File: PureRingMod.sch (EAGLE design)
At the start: 31 parts, among them IC1 TL074P, IC2 TL072P, X1 NC3FD-V

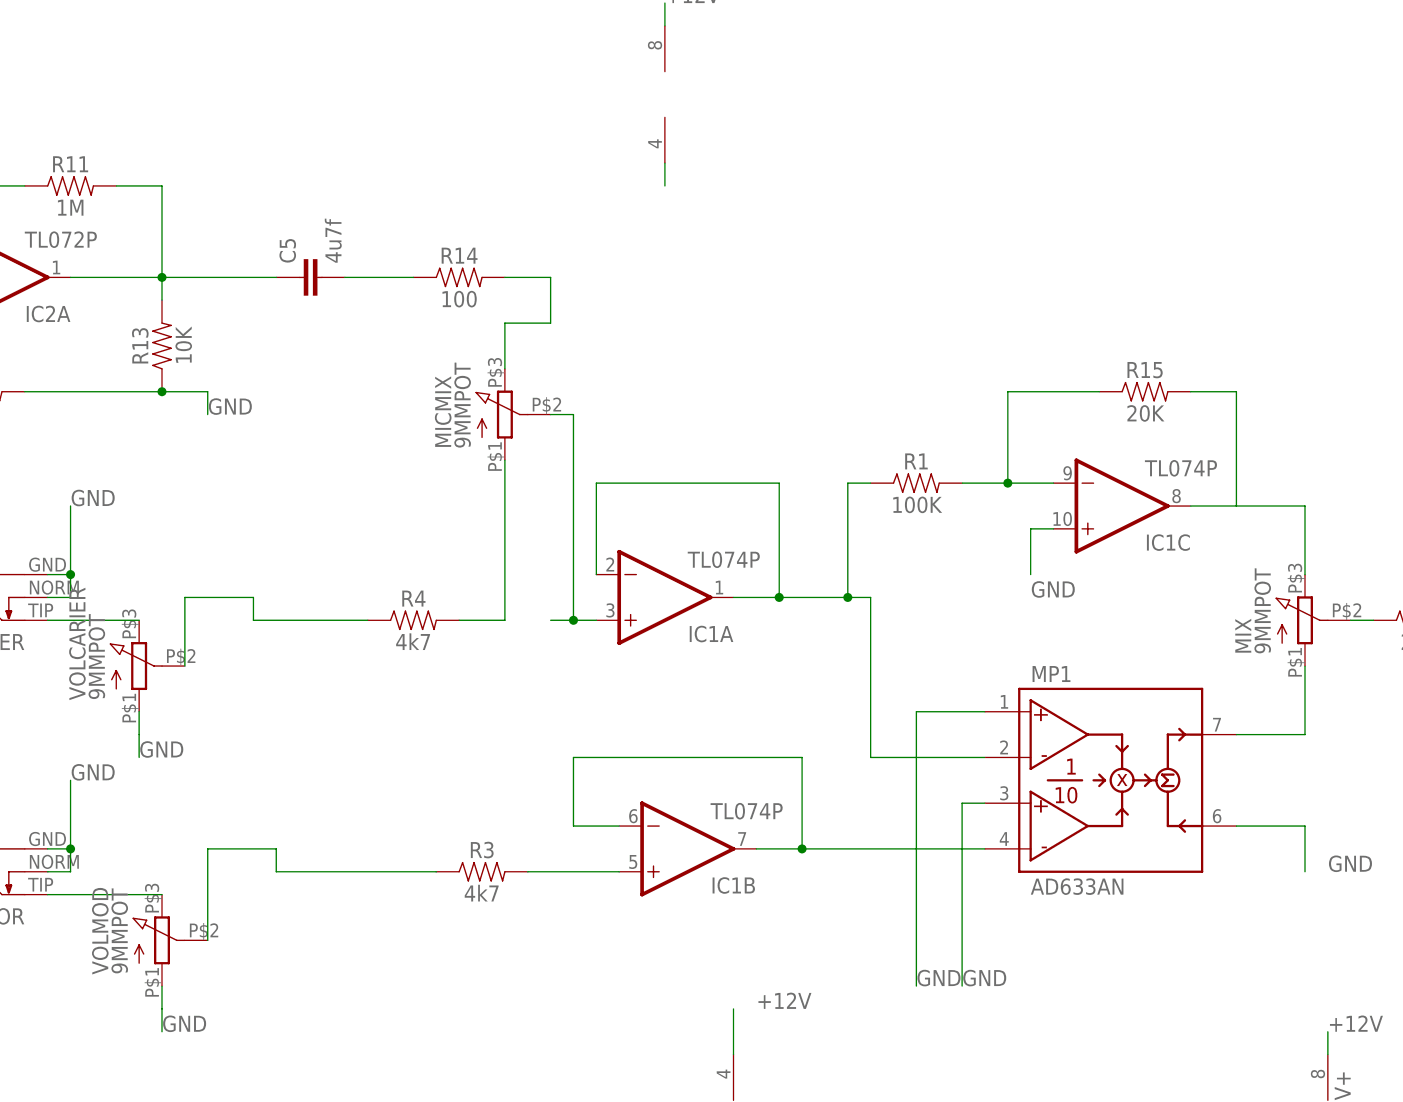
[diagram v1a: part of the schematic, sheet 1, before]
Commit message: Fixed wiring errors
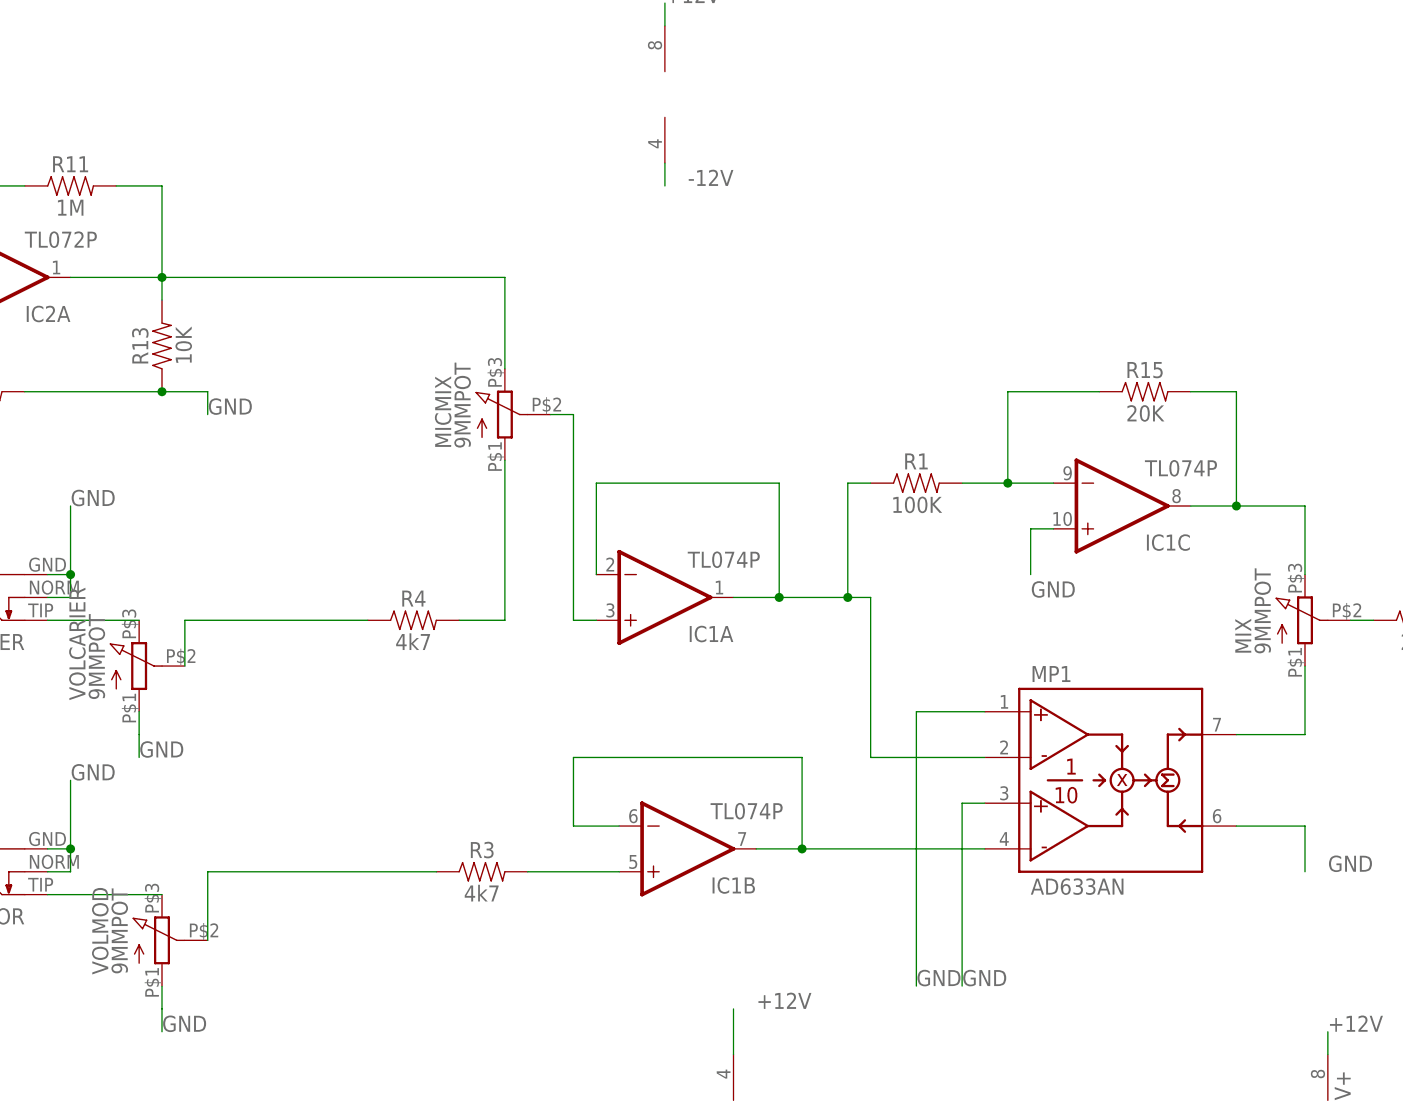
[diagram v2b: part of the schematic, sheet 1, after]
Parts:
- removed C5: 4u7f, SparkFun-Capacitors:0.1UF-KIT-EZ-50V-20%
- removed R14: 100, SparkFun-Resistors:330OHM-HORIZ-1/10W-5%
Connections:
- removed net N$26: C5.2, R14.1
- removed net N$29: MICMIX.3, R14.2
- new net N$8: MICMIX.1, R4.2
- net GND: no longer MICMIX.1, R4.2
- net N$27: now also MICMIX.3; no longer C5.1
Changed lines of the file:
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@@
 <part name="R10" library="SparkFun-Resistors" deviceset="330OHM" device="-HORIZ-1/10W-5%" value="27K"/>
 <part name="R11" library="SparkFun-Resistors" deviceset="330OHM" device="-HORIZ-1/10W-5%" value="1M"/>
-<part name="C5" library="SparkFun-Capacitors" deviceset="0.1UF" device="-KIT-EZ-50V-20%" value="4u7f"/>
 <part name="R12" library="SparkFun-Resistors" deviceset="330OHM" device="-HORIZ-1/10W-5%" value="1M"/>
 <part name="R13" library="SparkFun-Resistors" deviceset="330OHM" device="-HORIZ-1/10W-5%" value="10K"/>
-<part name="R14" library="SparkFun-Resistors" deviceset="330OHM" device="-HORIZ-1/10W-5%" value="100"/>
 <part name="MICMIX" library="GMSN" deviceset="9MMPOT" device=""/>
 <part name="R15" library="SparkFun-Resistors" deviceset="330OHM" device="-HORIZ-1/10W-5%" value="20K"/>
@@
 <attribute name="VALUE" x="-50.8" y="112.776" size="1.778" layer="96" font="vector" align="top-center"/>
 </instance>
-<instance part="C5" gate="G$1" x="-22.86" y="104.14" rot="R90">
-<attribute name="NAME" x="-25.781" y="105.664" size="1.778" layer="95" font="vector" rot="R90"/>
-<attribute name="VALUE" x="-20.701" y="105.664" size="1.778" layer="96" font="vector" rot="R90"/>
-</instance>
 <instance part="R12" gate="G$1" x="-60.96" y="91.44">
 <attribute name="NAME" x="-60.96" y="92.964" size="1.778" layer="95" font="vector" align="bottom-center"/>
@@
 <attribute name="NAME" x="-42.164" y="96.52" size="1.778" layer="95" font="vector" rot="R90" align="bottom-center"/>
 <attribute name="VALUE" x="-39.116" y="96.52" size="1.778" layer="96" font="vector" rot="R90" align="top-center"/>
-</instance>
-<instance part="R14" gate="G$1" x="-7.62" y="104.14">
-<attribute name="NAME" x="-7.62" y="105.664" size="1.778" layer="95" font="vector" align="bottom-center"/>
-<attribute name="VALUE" x="-7.62" y="102.616" size="1.778" layer="96" font="vector" align="top-center"/>
 </instance>
 <instance part="MICMIX" gate="G$1" x="-2.54" y="88.9" rot="R90">
@@
 <wire x1="-40.64" y1="91.44" x2="-55.88" y2="91.44" width="0.1524" layer="91"/>
 </segment>
-<segment>
-<pinref part="MICMIX" gate="G$1" pin="1"/>
-<pinref part="R4" gate="G$1" pin="2"/>
-<wire x1="-7.62" y1="66.04" x2="-2.54" y2="66.04" width="0.1524" layer="91"/>
-<wire x1="-2.54" y1="66.04" x2="-2.54" y2="83.82" width="0.1524" layer="91"/>
-</segment>
 </net>
 <net name="-12V" class="2">
@@
 <pinref part="IC2" gate="P" pin="V-"/>
 <wire x1="15.24" y1="116.84" x2="15.24" y2="114.3" width="0.1524" layer="91"/>
+<label x="17.78" y="114.3" size="1.778" layer="95"/>
 </segment>
 </net>
@@
 <wire x1="78.74" y1="91.44" x2="73.66" y2="91.44" width="0.1524" layer="91"/>
 <pinref part="R15" gate="G$1" pin="2"/>
+<junction x="78.74" y="78.74"/>
 </segment>
 </net>
@@
 <net name="N$18" class="0">
 <segment>
+<pinref part="R4" gate="G$1" pin="1"/>
+<wire x1="-38.1" y1="66.04" x2="-17.78" y2="66.04" width="0.1524" layer="91"/>
 <pinref part="VOLCARIER" gate="G$1" pin="2"/>
-<wire x1="-38.1" y1="60.96" x2="-38.1" y2="68.58" width="0.1524" layer="91"/>
-<wire x1="-38.1" y1="68.58" x2="-30.48" y2="68.58" width="0.1524" layer="91"/>
-<wire x1="-30.48" y1="68.58" x2="-30.48" y2="66.04" width="0.1524" layer="91"/>
-<pinref part="R4" gate="G$1" pin="1"/>
-<wire x1="-30.48" y1="66.04" x2="-17.78" y2="66.04" width="0.1524" layer="91"/>
+<wire x1="-38.1" y1="60.96" x2="-38.1" y2="66.04" width="0.1524" layer="91"/>
 </segment>
 </net>
 <net name="N$19" class="0">
 <segment>
+<pinref part="R3" gate="G$1" pin="1"/>
+<wire x1="-35.56" y1="38.1" x2="-10.16" y2="38.1" width="0.1524" layer="91"/>
 <pinref part="VOLMOD" gate="G$1" pin="2"/>
-<wire x1="-35.56" y1="30.48" x2="-35.56" y2="40.64" width="0.1524" layer="91"/>
-<wire x1="-27.94" y1="40.64" x2="-35.56" y2="40.64" width="0.1524" layer="91"/>
-<wire x1="-27.94" y1="40.64" x2="-27.94" y2="38.1" width="0.1524" layer="91"/>
-<pinref part="R3" gate="G$1" pin="1"/>
-<wire x1="-27.94" y1="38.1" x2="-10.16" y2="38.1" width="0.1524" layer="91"/>
+<wire x1="-35.56" y1="30.48" x2="-35.56" y2="38.1" width="0.1524" layer="91"/>
 </segment>
 </net>
@@
 <wire x1="-45.72" y1="114.3" x2="-40.64" y2="114.3" width="0.1524" layer="91"/>
 <wire x1="-40.64" y1="114.3" x2="-40.64" y2="104.14" width="0.1524" layer="91"/>
-<pinref part="C5" gate="G$1" pin="1"/>
-<wire x1="-40.64" y1="104.14" x2="-27.94" y2="104.14" width="0.1524" layer="91"/>
 <junction x="-40.64" y="104.14"/>
 <pinref part="R13" gate="G$1" pin="2"/>
 <wire x1="-40.64" y1="104.14" x2="-40.64" y2="101.6" width="0.1524" layer="91"/>
-</segment>
-</net>
-<net name="N$26" class="0">
-<segment>
-<pinref part="C5" gate="G$1" pin="2"/>
-<pinref part="R14" gate="G$1" pin="1"/>
-<wire x1="-20.32" y1="104.14" x2="-12.7" y2="104.14" width="0.1524" layer="91"/>
-</segment>
-</net>
-<net name="N$29" class="0">
-<segment>
-<pinref part="R14" gate="G$1" pin="2"/>
-<wire x1="-2.54" y1="104.14" x2="2.54" y2="104.14" width="0.1524" layer="91"/>
-<wire x1="2.54" y1="104.14" x2="2.54" y2="99.06" width="0.1524" layer="91"/>
-<wire x1="2.54" y1="99.06" x2="-2.54" y2="99.06" width="0.1524" layer="91"/>
+<wire x1="-40.64" y1="104.14" x2="-2.54" y2="104.14" width="0.1524" layer="91"/>
 <pinref part="MICMIX" gate="G$1" pin="3"/>
-<wire x1="-2.54" y1="99.06" x2="-2.54" y2="93.98" width="0.1524" layer="91"/>
+<wire x1="-2.54" y1="104.14" x2="-2.54" y2="93.98" width="0.1524" layer="91"/>
 </segment>
 </net>
@@
 <pinref part="IC1" gate="A" pin="+IN"/>
 <wire x1="7.62" y1="66.04" x2="5.08" y2="66.04" width="0.1524" layer="91"/>
-<wire x1="5.08" y1="66.04" x2="2.54" y2="66.04" width="0.1524" layer="91"/>
 <wire x1="5.08" y1="88.9" x2="5.08" y2="66.04" width="0.1524" layer="91"/>
-<junction x="5.08" y="66.04"/>
-</segment>
-</net>
+</segment>
+</net>
+<net name="N$8" class="0">
+<segment>
+<pinref part="MICMIX" gate="G$1" pin="1"/>
+<wire x1="-2.54" y1="83.82" x2="-2.54" y2="66.04" width="0.1524" layer="91"/>
+<pinref part="R4" gate="G$1" pin="2"/>
+<wire x1="-2.54" y1="66.04" x2="-7.62" y2="66.04" width="0.1524" layer="91"/>
+</segment>
+</net>

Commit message: V1.0 board
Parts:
- added GAIN: 9MMPOT, GMSN:9MMPOT
- added OUTPUT2: Output2, INSTRUO:S_JACK
- added R6: 1K, SparkFun-Resistors:330OHM-HORIZ-1/10W-5%
- R16: value 100K -> 10K
- R2: value 20K -> 10K
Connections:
- new net N$20: OUTPUT2.TIP, R6.2
- new net N$5: GAIN.1, R16.1
- net GND: now also OUTPUT2.GND
- net N$12: now also R6.1
- net N$7: now also GAIN.2, GAIN.3; no longer R16.1
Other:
- moved on the sheet: R16
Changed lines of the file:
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@@
 <part name="MIX" library="GMSN" deviceset="9MMPOT" device=""/>
 <part name="R1" library="SparkFun-Resistors" deviceset="330OHM" device="-HORIZ-1/10W-5%" value="100K"/>
-<part name="R2" library="SparkFun-Resistors" deviceset="330OHM" device="-HORIZ-1/10W-5%" value="20K"/>
+<part name="R2" library="SparkFun-Resistors" deviceset="330OHM" device="-HORIZ-1/10W-5%" value="10K"/>
 <part name="C4" library="SparkFun-Capacitors" deviceset="10UF-POLAR" device="-RADIAL-2.5MM-25V-20%" value="10uF"/>
 <part name="C1" library="SparkFun-Capacitors" deviceset="10UF-POLAR" device="-RADIAL-2.5MM-25V-20%" value="10uF"/>
@@
 <part name="MICMIX" library="GMSN" deviceset="9MMPOT" device=""/>
 <part name="R15" library="SparkFun-Resistors" deviceset="330OHM" device="-HORIZ-1/10W-5%" value="20K"/>
-<part name="R16" library="SparkFun-Resistors" deviceset="330OHM" device="-HORIZ-1/10W-5%" value="100K"/>
+<part name="R16" library="SparkFun-Resistors" deviceset="330OHM" device="-HORIZ-1/10W-5%" value="10K"/>
+<part name="GAIN" library="GMSN" deviceset="9MMPOT" device=""/>
+<part name="R6" library="SparkFun-Resistors" deviceset="330OHM" device="-HORIZ-1/10W-5%" value="1K"/>
+<part name="OUTPUT2" library="INSTRUO" deviceset="S_JACK" device="" value="Output2"/>
 </parts>
 <sheets>
@@
 <attribute name="VALUE" x="68.58" y="89.916" size="1.778" layer="96" font="vector" align="top-center"/>
 </instance>
-<instance part="R16" gate="G$1" x="114.3" y="78.74">
-<attribute name="NAME" x="114.3" y="80.264" size="1.778" layer="95" font="vector" align="bottom-center"/>
-<attribute name="VALUE" x="114.3" y="77.216" size="1.778" layer="96" font="vector" align="top-center"/>
+<instance part="R16" gate="G$1" x="119.38" y="78.74">
+<attribute name="NAME" x="119.38" y="80.264" size="1.778" layer="95" font="vector" align="bottom-center"/>
+<attribute name="VALUE" x="119.38" y="77.216" size="1.778" layer="96" font="vector" align="top-center"/>
+</instance>
+<instance part="GAIN" gate="G$1" x="109.22" y="78.74" rot="R180">
+<attribute name="NAME" x="113.03" y="72.771" size="1.778" layer="95" rot="R180"/>
+<attribute name="VALUE" x="113.03" y="74.93" size="1.778" layer="96" rot="R180"/>
+</instance>
+<instance part="R6" gate="G$1" x="132.08" y="45.72">
+<attribute name="NAME" x="132.08" y="47.244" size="1.778" layer="95" font="vector" align="bottom-center"/>
+<attribute name="VALUE" x="132.08" y="44.196" size="1.778" layer="96" font="vector" align="top-center"/>
+</instance>
+<instance part="OUTPUT2" gate="G$1" x="157.48" y="45.72">
+<attribute name="NAME" x="154.94" y="49.784" size="1.778" layer="95"/>
+<attribute name="VALUE" x="154.94" y="39.624" size="1.778" layer="96"/>
 </instance>
 </instances>
@@
 <wire x1="-40.64" y1="91.44" x2="-55.88" y2="91.44" width="0.1524" layer="91"/>
 </segment>
+<segment>
+<pinref part="OUTPUT2" gate="G$1" pin="GND"/>
+<wire x1="152.4" y1="43.18" x2="149.86" y2="43.18" width="0.1524" layer="91"/>
+<wire x1="149.86" y1="43.18" x2="149.86" y2="40.64" width="0.1524" layer="91"/>
+<label x="149.86" y="38.1" size="1.778" layer="95"/>
+</segment>
 </net>
 <net name="-12V" class="2">
@@
 </segment>
 </net>
-<net name="N$5" class="0">
-<segment>
-<pinref part="R1" gate="G$1" pin="2"/>
-<pinref part="IC1" gate="C" pin="-IN"/>
-<wire x1="48.26" y1="81.28" x2="53.34" y2="81.28" width="0.1524" layer="91"/>
-<wire x1="53.34" y1="81.28" x2="58.42" y2="81.28" width="0.1524" layer="91"/>
-<wire x1="53.34" y1="91.44" x2="53.34" y2="81.28" width="0.1524" layer="91"/>
-<junction x="53.34" y="81.28"/>
-<wire x1="53.34" y1="91.44" x2="63.5" y2="91.44" width="0.1524" layer="91"/>
-<pinref part="R15" gate="G$1" pin="1"/>
-</segment>
-</net>
 <net name="N$6" class="0">
 <segment>
@@
 <wire x1="104.14" y1="66.04" x2="104.14" y2="78.74" width="0.1524" layer="91"/>
 <junction x="104.14" y="66.04"/>
-<pinref part="R16" gate="G$1" pin="1"/>
-<wire x1="104.14" y1="78.74" x2="109.22" y2="78.74" width="0.1524" layer="91"/>
+<pinref part="GAIN" gate="G$1" pin="3"/>
+<pinref part="GAIN" gate="G$1" pin="2"/>
+<wire x1="109.22" y1="83.82" x2="109.22" y2="86.36" width="0.1524" layer="91"/>
+<wire x1="109.22" y1="86.36" x2="104.14" y2="86.36" width="0.1524" layer="91"/>
+<wire x1="104.14" y1="86.36" x2="104.14" y2="78.74" width="0.1524" layer="91"/>
+<junction x="104.14" y="78.74"/>
 </segment>
 </net>
@@
 <junction x="124.46" y="63.5"/>
 <pinref part="R16" gate="G$1" pin="2"/>
-<wire x1="119.38" y1="78.74" x2="124.46" y2="78.74" width="0.1524" layer="91"/>
+<pinref part="R6" gate="G$1" pin="1"/>
+<wire x1="124.46" y1="45.72" x2="127" y2="45.72" width="0.1524" layer="91"/>
+<wire x1="124.46" y1="63.5" x2="124.46" y2="45.72" width="0.1524" layer="91"/>
 </segment>
 </net>
@@
 </segment>
 </net>
+<net name="N$14" class="0">
+<segment>
+<pinref part="IC1" gate="C" pin="-IN"/>
+<pinref part="R1" gate="G$1" pin="2"/>
+<wire x1="48.26" y1="81.28" x2="55.88" y2="81.28" width="0.1524" layer="91"/>
+<pinref part="R15" gate="G$1" pin="1"/>
+<wire x1="55.88" y1="81.28" x2="58.42" y2="81.28" width="0.1524" layer="91"/>
+<wire x1="63.5" y1="91.44" x2="55.88" y2="91.44" width="0.1524" layer="91"/>
+<wire x1="55.88" y1="91.44" x2="55.88" y2="81.28" width="0.1524" layer="91"/>
+<junction x="55.88" y="81.28"/>
+</segment>
+</net>
+<net name="N$5" class="0">
+<segment>
+<pinref part="R16" gate="G$1" pin="1"/>
+<pinref part="GAIN" gate="G$1" pin="1"/>
+</segment>
+</net>
+<net name="N$20" class="0">
+<segment>
+<pinref part="R6" gate="G$1" pin="2"/>
+<wire x1="137.16" y1="45.72" x2="139.7" y2="45.72" width="0.1524" layer="91"/>
+<wire x1="139.7" y1="45.72" x2="139.7" y2="48.26" width="0.1524" layer="91"/>
+<pinref part="OUTPUT2" gate="G$1" pin="TIP"/>
+<wire x1="139.7" y1="48.26" x2="152.4" y2="48.26" width="0.1524" layer="91"/>
+</segment>
+</net>

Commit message: updated BOM
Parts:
- D1: value (none) -> 1n4148
- D2: value (none) -> 1N4148
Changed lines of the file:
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@@
 <part name="MP1" library="ad633-2" deviceset="AD633*" device="N" technology="A"/>
 <part name="IC1" library="GMSN" deviceset="TL074" device="P"/>
-<part name="D1" library="adafruit" deviceset="DIODE" device="DO-1N4148"/>
-<part name="D2" library="adafruit" deviceset="DIODE" device="DO-1N4148"/>
+<part name="D1" library="adafruit" deviceset="DIODE" device="DO-1N4148" value="1n4148"/>
+<part name="D2" library="adafruit" deviceset="DIODE" device="DO-1N4148" value="1N4148"/>
 <part name="SUPPLY4" library="supply2" deviceset="+12V" device=""/>
 <part name="SUPPLY5" library="supply2" deviceset="-12V" device=""/>
